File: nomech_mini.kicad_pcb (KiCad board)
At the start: 2 copper layers, 63 x 63 mm, 107 parts, among them CON1 USB_2B, CON2 AVR-ISP-6, P1 CONN_1, P2 CONN_1, P3 CONN_1, P4 CONN_1, P5 CONN_1, Q1 MOSFET_N, Q2 MOSFET_N, Q3 MOSFET_N, Q4 MOSFET_N, U1 ATMEGA32U4, X1 CRYSTAL_16MHz

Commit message: routing... ugly but nice
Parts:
- moved R9 76.5 mm to (138.7, 92.0)
- moved R7 76.3 mm to (136.5, 92.0)
- moved R8 11.1 mm to (164.5, 91.2)
- moved C6 10.2 mm to (120.3, 107.4)
- moved R6 8.37 mm to (164.5, 96.8)
- moved L2 8.20 mm to (118.7, 105.4)
- moved R4 6.39 mm to (164.5, 102.2)
- moved Q4 6.16 mm to (164.8, 88.5)
- moved R39 6.06 mm to (160.8, 89.8)
- moved R40 6.06 mm to (160.8, 87.8)
- moved R3 5.90 mm to (164.5, 107.8)
- moved C18 5.40 mm to (168.0, 88.5)
- moved Q3 5.19 mm to (164.8, 94.0)
- moved R33 5.09 mm to (161.0, 95.0)
- moved R38 5.09 mm to (161.0, 93.0)
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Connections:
- R3 pad 1: N-0000035 -> N-0000030
- R4 pad 1: N-0000034 -> N-0000029
- R6 pad 1: N-0000033 -> N-0000028
- R8 pad 1: N-0000032 -> N-0000027
- U1 pad 30: N-0000032 -> N-0000030
- U1 pad 31: N-0000033 -> N-0000029
- U1 pad 32: N-0000034 -> N-0000028
- U1 pad 33: N-0000035 -> N-0000027
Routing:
- net N-0000027: track 0.00 -> 36.6 mm, vias 0 -> 1
- net N-000006: track 36.5 -> 0.00 mm, vias 2 -> 0
- net N-0000028: track 0.00 -> 35.4 mm, vias 0 -> 1
- net N-0000035: track 35.1 -> 0.00 mm, vias 2 -> 0
- net N-0000029: track 0.00 -> 34.3 mm, vias 0 -> 1
- net N-0000034: track 33.7 -> 0.00 mm, vias 2 -> 0
- net N-0000030: track 0.00 -> 33.5 mm, vias 0 -> 1
- net N-0000033: track 32.8 -> 0.00 mm, vias 2 -> 0
- net N-0000032: track 32.8 -> 0.00 mm, vias 2 -> 0
- net N-0000038: track 0.00 -> 28.6 mm, vias 0 -> 1
- net /ISP_SCK: track 0.00 -> 28.0 mm, vias 0 -> 1
- net N-0000025: track 2.69 -> 28.9 mm
- net /ISP_MOSI: track 0.00 -> 26.2 mm, vias 0 -> 1
- net LED_COLUMN_3: track 25.6 -> 48.5 mm, vias 2 -> 1
- net LED_COLUMN_2: track 26.9 -> 49.6 mm, vias 2 -> 1
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
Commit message: routing... nicely
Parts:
- moved C14 28.1 mm to (140.7, 96.9), turned to 180 degrees
- moved C11 28.0 mm to (140.7, 94.8)
- moved C4 22.8 mm to (132.7, 90.5), turned to 135 degrees
- moved R3 5.35 mm to (167.8, 103.5)
- moved R4 4.96 mm to (167.8, 98.5)
- moved R6 4.60 mm to (167.8, 93.5)
- moved R8 4.26 mm to (167.8, 88.5)
- moved Q4 4.10 mm to (168.0, 91.0)
- moved R39 4.10 mm to (164.0, 92.2)
- moved R40 4.10 mm to (164.0, 90.2)
- moved C18 4.05 mm to (171.1, 91.1)
- moved C17 3.82 mm to (171.2, 96.0)
- moved Q3 3.82 mm to (168.0, 96.0)
- moved R33 3.82 mm to (164.2, 97.0)
- moved R38 3.82 mm to (164.2, 95.0)
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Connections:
- U1 pad 18: LED_COLUMN_1 -> LED_COLUMN_4
- U1 pad 19: LED_COLUMN_2 -> LED_COLUMN_3
- U1 pad 20: LED_COLUMN_3 -> LED_COLUMN_2
- U1 pad 21: LED_COLUMN_4 -> LED_COLUMN_1
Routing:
- net X4: track 0.00 -> 91.9 mm, vias 0 -> 1
- net LED_ROW_4_SW: track 0.00 -> 87.9 mm
- net X3: track 0.00 -> 70.8 mm, vias 0 -> 1
- net LED_ROW_3_SW: track 0.00 -> 65.1 mm
- net LED_COLUMN_1: track 50.9 -> 104.3 mm, vias 1 -> 2
- net X2: track 0.00 -> 46.3 mm, vias 0 -> 1
- net LED_ROW_2_SW: track 0.00 -> 43.0 mm
- net LED_COLUMN_2: track 49.6 -> 88.2 mm, vias 1 -> 2
- net N-0000025: track 28.9 -> 0.00 mm, vias 1 -> 0
- net LED_COLUMN_3: track 48.5 -> 72.5 mm, vias 1 -> 2
- net X1: track 0.00 -> 23.9 mm, vias 0 -> 1
- net N-0000027: track 36.6 -> 59.6 mm, vias 1 -> 2
- net N-0000028: track 35.4 -> 55.4 mm, vias 1 -> 2
- net LED_ROW_1_SW: track 0.00 -> 18.9 mm
- net N-0000029: track 34.3 -> 50.5 mm, vias 1 -> 2
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
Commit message: routing.. SPI done
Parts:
- added C19: 100nF, SM0805, B.Cu at (117.6, 96.0)
- added C20: 10nF, SM0805, B.Cu at (119.4, 98.0)
- moved CON2 43.2 mm to (154.4, 87.9)
- moved P4 41.2 mm to (149.4, 86.6)
- moved C12 16.4 mm to (133.9, 89.7)
- moved C13 16.2 mm to (132.1, 89.7)
- moved D1 5.57 mm to (147.4, 95.5)
- moved R1 5.57 mm to (147.4, 92.8)
- moved C11 4.74 mm to (140.7, 99.6), turned to 90 degrees
- moved C4 4.11 mm to (132.3, 86.4)
- moved C14 3.35 mm to (138.7, 99.6), turned to 90 degrees
- moved R9 3.00 mm to (136.4, 94.0), turned to 180 degrees
- moved R7 0.18 mm to (136.4, 92.2), turned to 180 degrees
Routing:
- net +5V: track 3.34 -> 54.8 mm, vias 1 -> 2
- net /ISP_MOSI: track 26.2 -> 49.8 mm
- net N-0000038: track 28.6 -> 51.2 mm
- net /ISP_RST: track 20.8 -> 37.8 mm, vias 1 -> 2
- net /ISP_SCK: track 28.0 -> 44.7 mm
- net /ISP_MISO: track 21.9 -> 34.2 mm, vias 1 -> 2
- net N-0000015: track 0.00 -> 5.49 mm
- net N-0000014: track 0.00 -> 5.31 mm

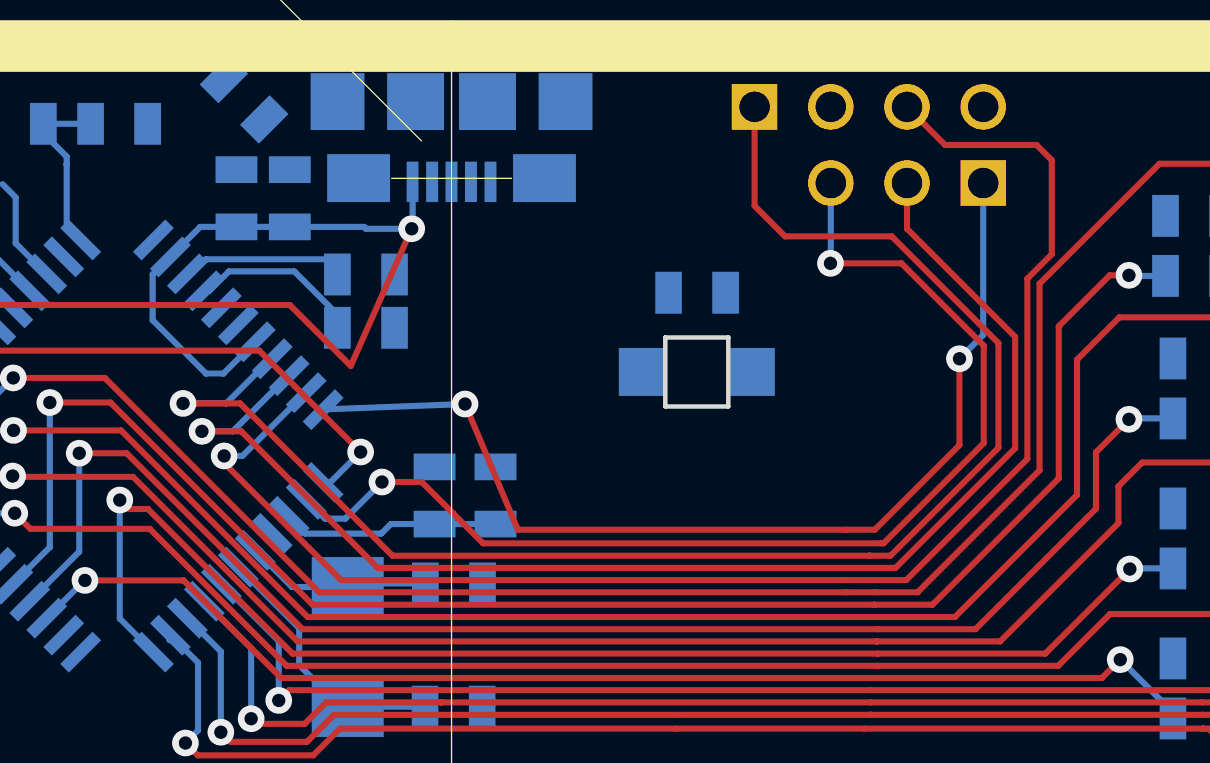
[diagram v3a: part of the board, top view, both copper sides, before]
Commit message: SPI tear-up and re-route
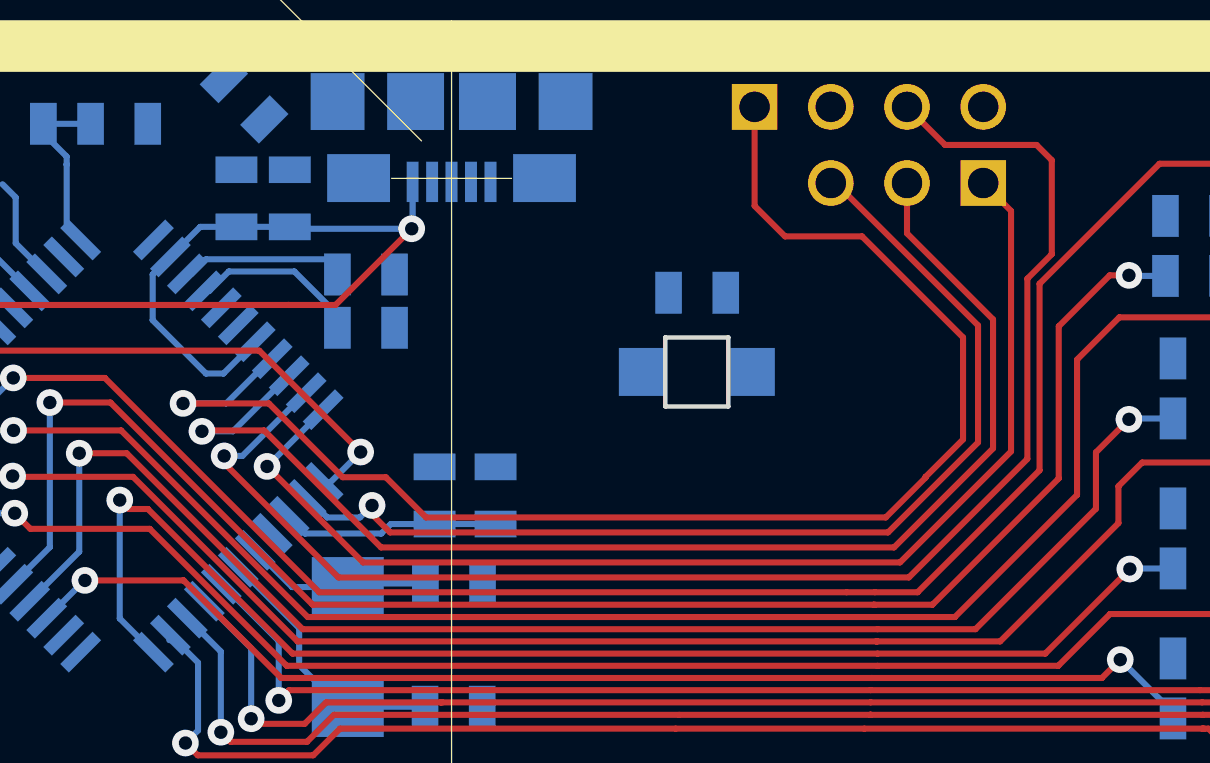
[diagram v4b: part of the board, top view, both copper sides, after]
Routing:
- net /ISP_MISO: track 34.2 -> 39.7 mm, vias 2 -> 1
- net N-0000038: track 51.2 -> 47.7 mm
- net +5V: track 54.8 -> 52.3 mm
- net /ISP_RST: track 37.8 -> 35.5 mm, vias 2 -> 1
- net /ISP_SCK: track 44.7 -> 43.1 mm

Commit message: routing, grounds on outside
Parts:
- removed P1, P2, P3, P5: CONN_1, PIN_ARRAY_1
- added GND1: GND, TEST_POINT_2PADS, F.Cu at (115.2, 86.5)
- added VCC1: +5V, TEST_POINT_2PADS, F.Cu at (162.4, 86.5)
- E1, E10, E11, E12, E13, E14, E15, E16, E2, E3, E4, E5, E6, E7, E8, E9: footprint cap-electrode_16mm_reverseLED -> cap-electrode_16mm_reverseLED3
- moved R13 52.6 mm to (150.0, 93.0), turned to 0 degrees
- moved C4 8.96 mm to (136.3, 94.4), turned to 315 degrees
- moved C6 5.55 mm to (125.8, 106.9)
- moved R7 3.90 mm to (140.3, 92.1)
- moved R9 3.90 mm to (140.3, 93.9)
- moved L2 3.87 mm to (122.5, 104.9), turned to 0 degrees
- moved C2 2.74 mm to (124.1, 88.8)
- moved L1 1.77 mm to (128.8, 88.8)
- moved C1 1.58 mm to (126.1, 87.8), turned to 270 degrees
- moved R1 0.93 mm to (146.5, 93.0), turned to 180 degrees
- turned R26 to 180 degrees
- turned R32 to 180 degrees
- turned R38 to 180 degrees
- turned R40 to 180 degrees
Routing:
- net GND: track 0.00 -> 434.5 mm, vias 0 -> 57
- net (no net): track 101.9 -> 0.00 mm, vias 11 -> 0
- net LED_ROW_3_SW: track 65.1 -> 149.1 mm, vias 0 -> 4
- net LED_ROW_2_SW: track 43.0 -> 127.0 mm, vias 0 -> 4
- net LED_ROW_1_SW: track 18.9 -> 102.9 mm, vias 0 -> 4
- net LED_ROW_4_SW: track 87.9 -> 148.3 mm
- net +5V: track 52.3 -> 112.7 mm, vias 2 -> 5
- net LED_COLUMN_3: track 72.5 -> 128.6 mm
- net LED_COLUMN_2: track 88.2 -> 144.1 mm
- net Y1: track 15.1 -> 71.1 mm, vias 1 -> 7
- net LED_COLUMN_4: track 56.6 -> 112.5 mm
- net LED_COLUMN_1: track 104.3 -> 160.0 mm
- net Y4: track 55.8 -> 106.8 mm, vias 1 -> 7
- net Y3: track 41.6 -> 92.6 mm, vias 1 -> 7
- net Y2: track 27.7 -> 78.7 mm, vias 1 -> 7
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- added copper zone on B.Cu, net GND
- added copper zone on F.Cu, net GND
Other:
- board size 63 x 63 mm -> 2.1 x 2.3 mm

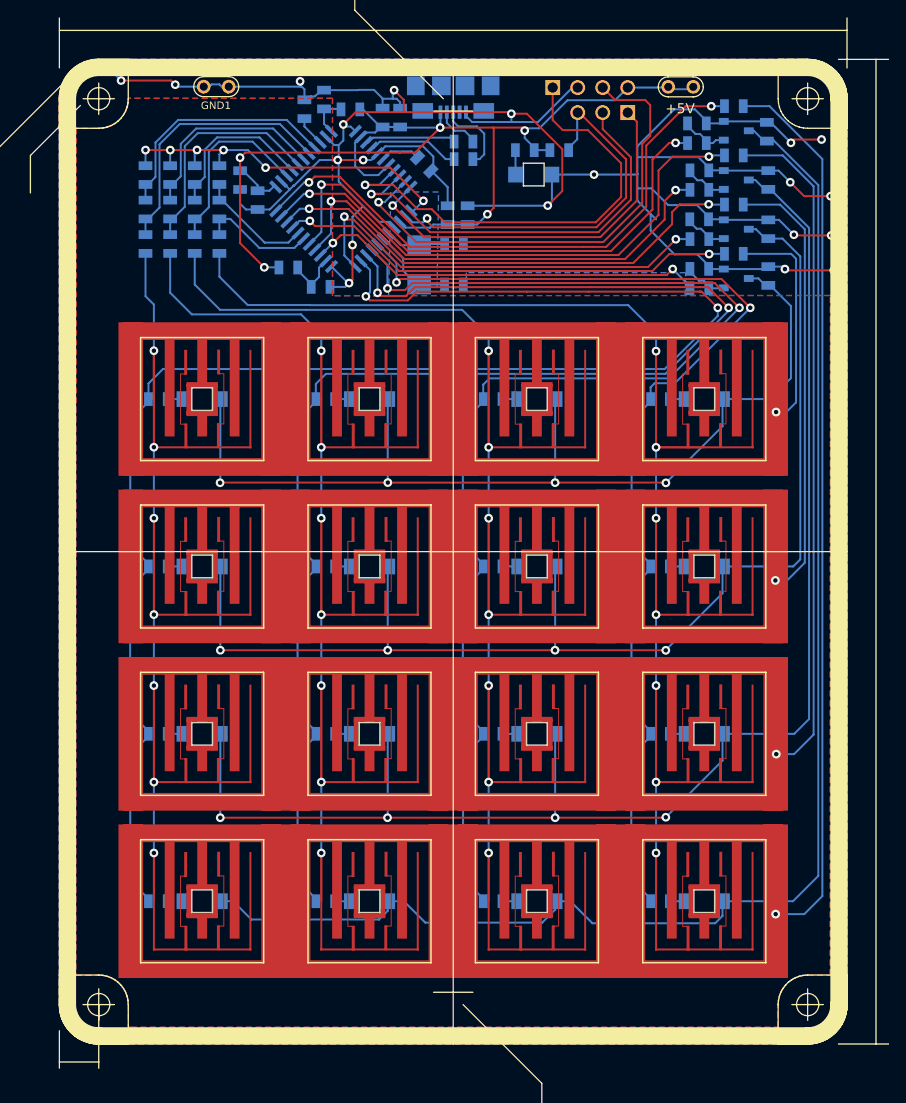
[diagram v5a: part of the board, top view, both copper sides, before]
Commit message: routing, smaller ground plane
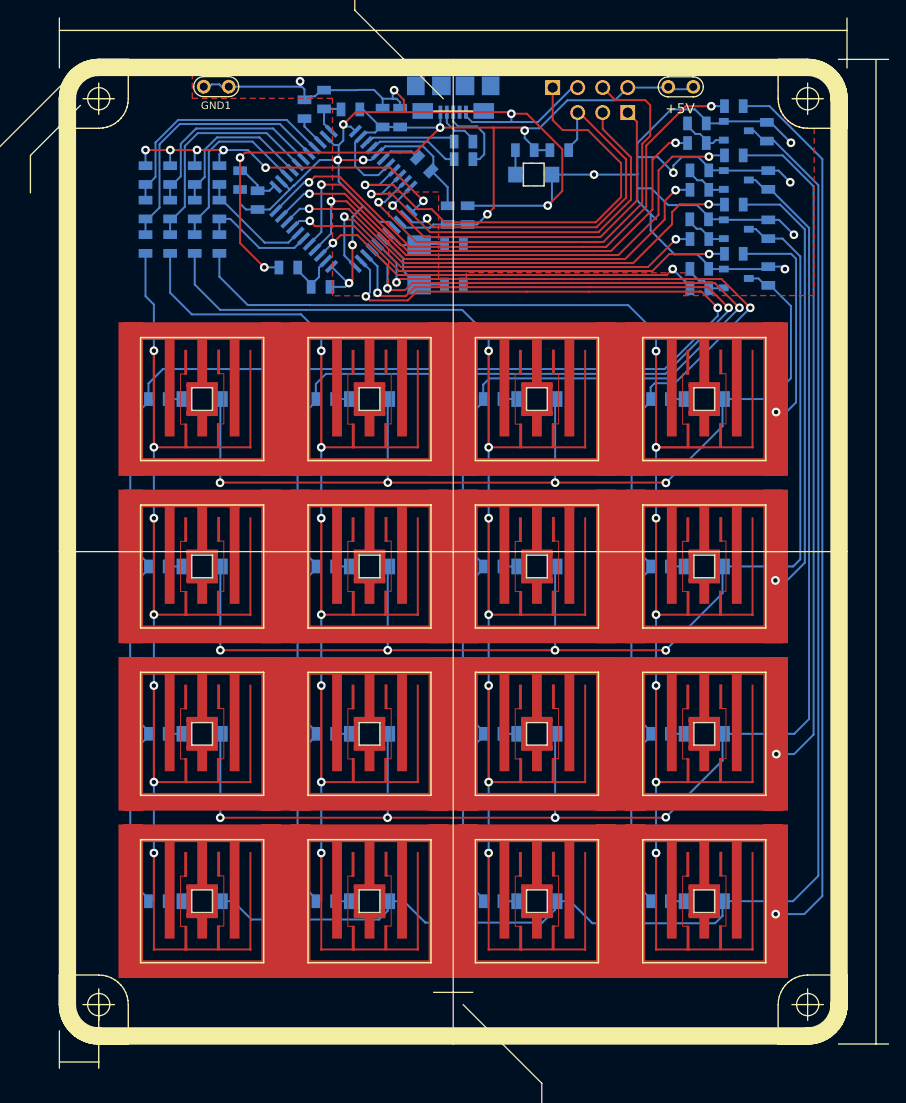
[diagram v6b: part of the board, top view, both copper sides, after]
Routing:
- net GND: track 434.5 -> 238.4 mm, vias 57 -> 15

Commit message: adding BOM, routing... ground planes
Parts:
- DP10080_v1: footprint dp_pcb-DP10080_V1 -> dp_pcb-DP10080_V1_2
- moved CON1 1.19 mm to (139.2, 83.8)
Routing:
- net GND: track 238.4 -> 245.9 mm, vias 15 -> 18
- net N-0000020: track 4.67 -> 5.86 mm
- net N-0000018: track 8.05 -> 9.24 mm
- net +5V: track 112.7 -> 113.9 mm
- net N-0000031: track 50.5 -> 50.0 mm

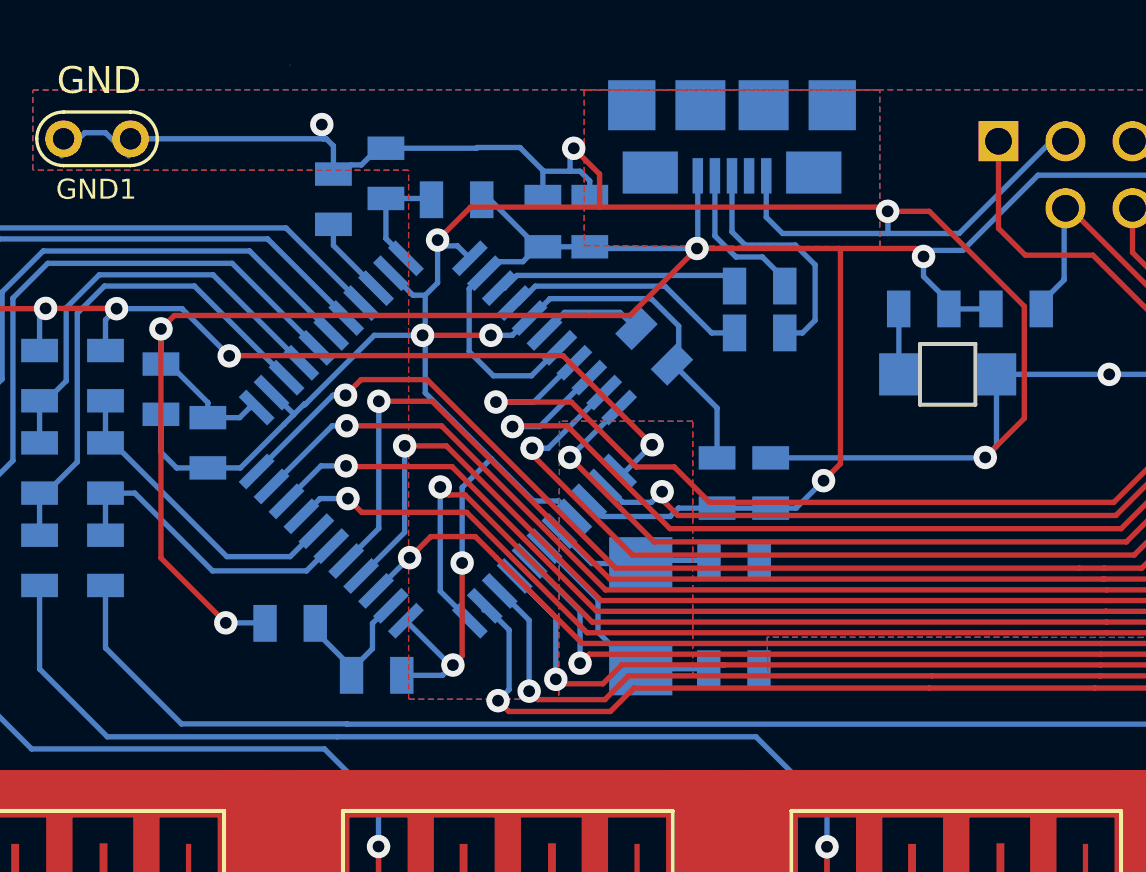
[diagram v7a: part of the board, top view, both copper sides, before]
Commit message: some minor placing and routing corrections
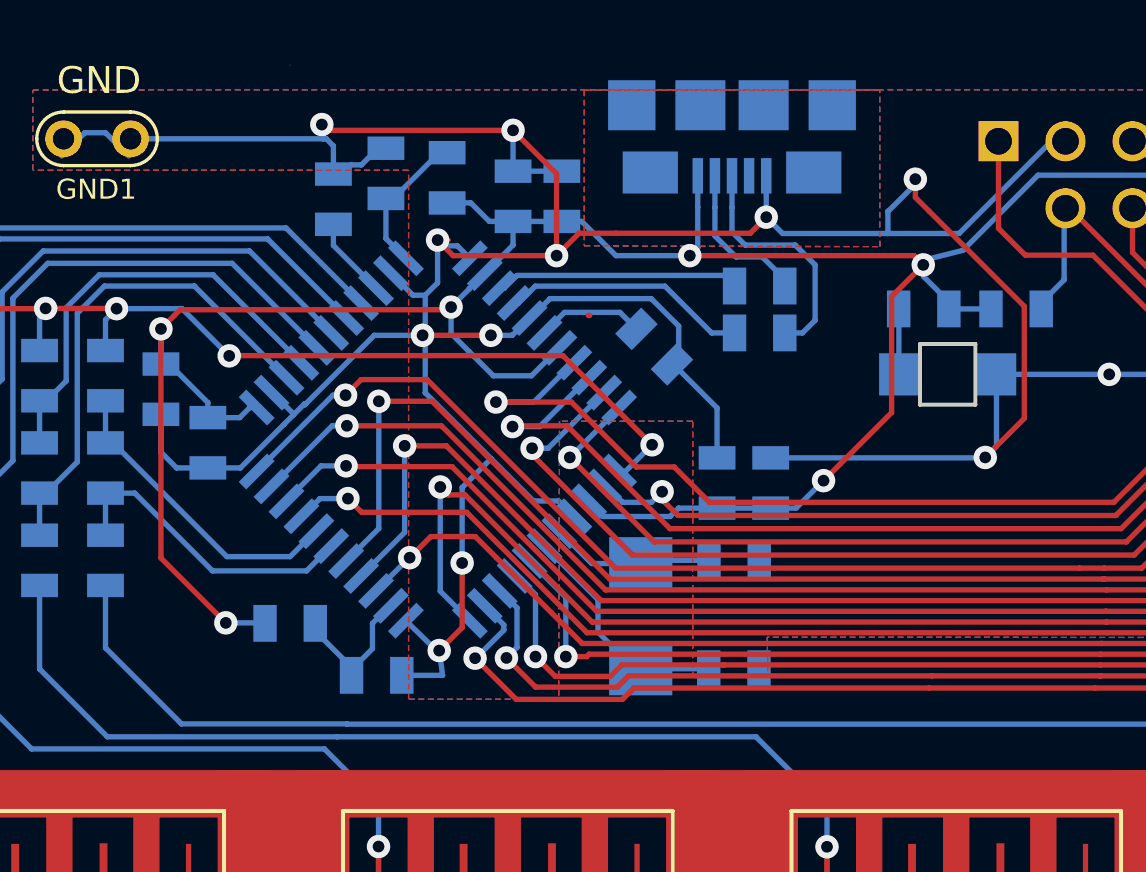
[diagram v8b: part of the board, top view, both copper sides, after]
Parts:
- C1, C10, C11, C12, C13, C14, C15, C16, C17, C18, C19, C2, C20, C3, C4, C5, C6, C7, C8, C9, L1, L2, R1, R10, R11, R12, R13, R14, R15, R16, R17, R18, R19, R2, R20, R21, R22, R23, R24, R25, R26, R27, R28, R29, R3, R30, R31, R32, R33, R34, R35, R36, R37, R38, R39, R4, R40, R5, R6, R7, R8, R9: footprint SM0805 -> SM0805_nop
- moved C13 1.48 mm to (130.9, 88.7)
- moved C12 1.43 mm to (132.8, 88.7)
- moved L1 0.90 mm to (128.4, 88.0), turned to 90 degrees
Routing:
- net +5V: track 113.9 -> 107.3 mm, vias 5 -> 6
- net N-0000026: track 4.98 -> 6.31 mm
- net GND: track 245.9 -> 245.7 mm, vias 18 -> 20
